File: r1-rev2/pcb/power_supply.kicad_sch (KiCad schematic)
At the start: 28 parts, among them J5 GT-BTP30003-xxxA-16A, Q3 AO3401A, U4 LM66100DCK, U5 TPS62A01DRLR, U6 TPS62A01DRLR, U7 AP2125K-3.0, U8 AP2125K-3.0, U9 TP4057

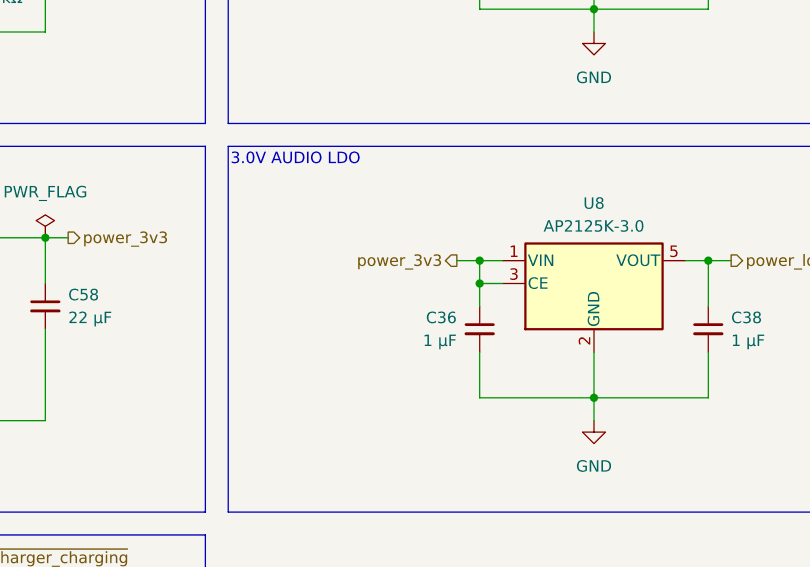
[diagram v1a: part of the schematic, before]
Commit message: R1-Rev2: use LDO enable pin to control codec AVDD supply
Now that the codec has a dedicated power supply for AVDD,
the LDO's enable pin can be used for power sequencing.
This eliminates a resistor and PMOS.
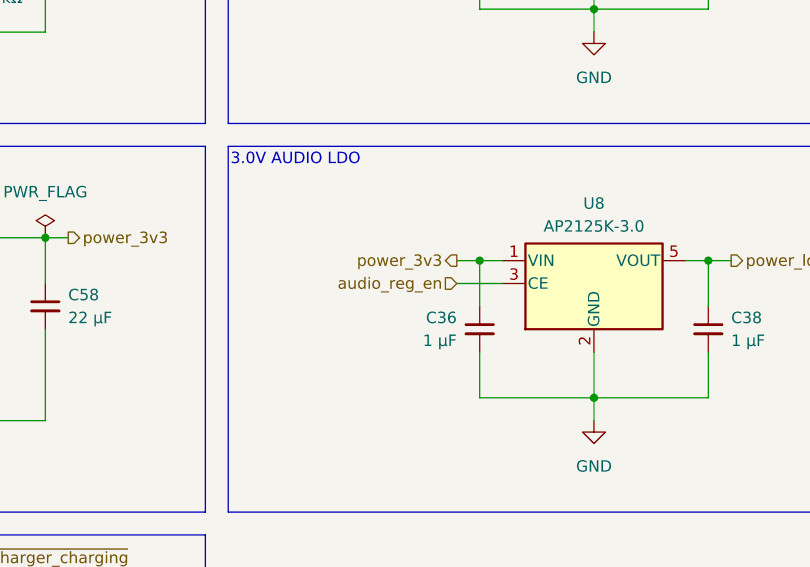
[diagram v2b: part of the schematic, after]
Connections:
- net power_3v3: no longer U8.3 (CE)
- new net audio_reg_en: U8.3 (CE)
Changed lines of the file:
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@@
-	)
-	(junction
-		(at 213.36 91.44)
-		(diameter 0)
-		(color 0 0 0 0)
 	)
 	(junction
@@
 	(wire
 		(pts
-			(xy 213.36 88.9) (xy 213.36 91.44)
+			(xy 213.36 88.9) (xy 213.36 93.98)
 		)
 		(stroke
@@
 	(wire
 		(pts
+			(xy 210.82 91.44) (xy 215.9 91.44)
+		)
+		(stroke
+			(width 0)
+			(type default)
+		)
+	)
+	(wire
+		(pts
 			(xy 121.92 106.68) (xy 132.08 106.68)
 		)
@@
 	(wire
 		(pts
-			(xy 213.36 91.44) (xy 215.9 91.44)
-		)
-		(stroke
-			(width 0)
-			(type default)
-		)
-	)
-	(wire
-		(pts
 			(xy 226.06 99.06) (xy 226.06 104.14)
 		)
@@
 		(pts
 			(xy 114.3 45.72) (xy 124.46 45.72)
-		)
-		(stroke
-			(width 0)
-			(type default)
-		)
-	)
-	(wire
-		(pts
-			(xy 213.36 91.44) (xy 213.36 93.98)
 		)
 		(stroke
@@
 		)
 	)
+	(hierarchical_label "audio_reg_en"
+		(shape input)
+		(at 210.82 91.44 180)
+		(effects
+			(font
+				(size 1.27 1.27)
+			)
+			(justify right)
+		)
+	)

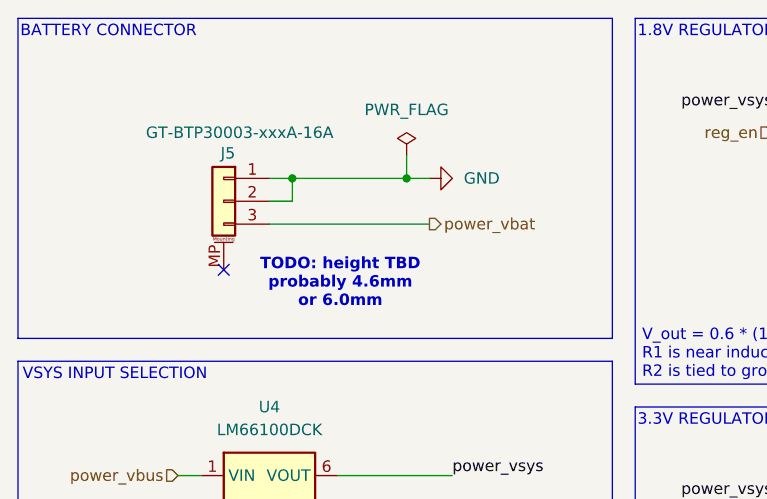
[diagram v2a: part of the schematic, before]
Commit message: R1-Rev2: add optional connection point for a wired battery
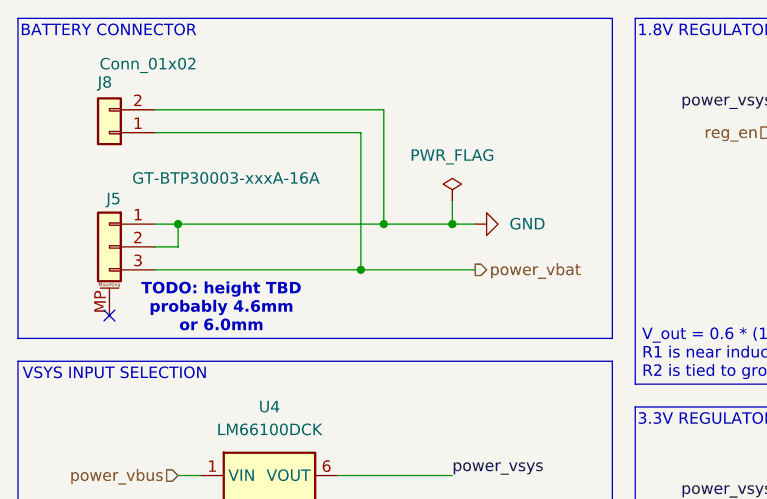
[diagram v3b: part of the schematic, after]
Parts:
- added J8: Conn_01x02, Connector_PinHeader_2.54mm:PinHeader_1x02_P2.54mm_Vertical, symbol Connector_Generic:Conn_01x02
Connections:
- net GND: now also J8.2 (Pin_2)
- net power_vbat: now also J8.1 (Pin_1)
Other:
- moved on the sheet: J5
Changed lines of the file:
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@@
 	(text "TODO: height TBD\nprobably 4.6mm\nor 6.0mm"
 		(exclude_from_sim no)
-		(at 66.294 62.484 0)
+		(at 53.086 65.278 0)
 		(effects
 			(font
@@
 	)
 	(junction
+		(at 68.58 60.96)
+		(diameter 0)
+		(color 0 0 0 0)
+	)
+	(junction
 		(at 149.86 86.36)
 		(diameter 0)
@@
 	)
 	(junction
+		(at 71.12 55.88)
+		(diameter 0)
+		(color 0 0 0 0)
+	)
+	(junction
 		(at 165.1 134.62)
 		(diameter 0)
@@
 	)
 	(junction
-		(at 73.66 50.8)
-		(diameter 0)
-		(color 0 0 0 0)
-	)
-	(junction
 		(at 149.86 106.68)
 		(diameter 0)
@@
 	)
 	(junction
-		(at 60.96 50.8)
+		(at 48.26 55.88)
 		(diameter 0)
 		(color 0 0 0 0)
@@
 	)
 	(junction
+		(at 78.74 55.88)
+		(diameter 0)
+		(color 0 0 0 0)
+	)
+	(junction
 		(at 213.36 45.72)
 		(diameter 0)
@@
 	)
 	(no_connect
-		(at 53.34 60.96)
+		(at 40.64 66.04)
 	)
 	(wire
@@
 	(wire
 		(pts
-			(xy 73.66 48.26) (xy 73.66 50.8)
-		)
-		(stroke
-			(width 0)
-			(type default)
-		)
-	)
-	(wire
-		(pts
 			(xy 132.08 106.68) (xy 132.08 109.22)
 		)
@@
 	(wire
 		(pts
+			(xy 45.72 43.18) (xy 71.12 43.18)
+		)
+		(stroke
+			(width 0)
+			(type default)
+		)
+	)
+	(wire
+		(pts
 			(xy 238.76 45.72) (xy 241.3 45.72)
 		)
@@
 	(wire
 		(pts
+			(xy 45.72 45.72) (xy 68.58 45.72)
+		)
+		(stroke
+			(width 0)
+			(type default)
+		)
+	)
+	(wire
+		(pts
 			(xy 210.82 88.9) (xy 213.36 88.9)
 		)
@@
 	(wire
 		(pts
-			(xy 58.42 55.88) (xy 76.2 55.88)
+			(xy 45.72 60.96) (xy 68.58 60.96)
 		)
 		(stroke
@@
 	(wire
 		(pts
+			(xy 78.74 55.88) (xy 78.74 53.34)
+		)
+		(stroke
+			(width 0)
+			(type default)
+		)
+	)
+	(wire
+		(pts
 			(xy 127 149.86) (xy 139.7 149.86)
 		)
@@
 	(wire
 		(pts
+			(xy 78.74 55.88) (xy 81.28 55.88)
+		)
+		(stroke
+			(width 0)
+			(type default)
+		)
+	)
+	(wire
+		(pts
 			(xy 144.78 96.52) (xy 149.86 96.52)
 		)
@@
 	(wire
 		(pts
-			(xy 58.42 53.34) (xy 60.96 53.34)
+			(xy 45.72 58.42) (xy 48.26 58.42)
 		)
 		(stroke
@@
 	(wire
 		(pts
-			(xy 60.96 50.8) (xy 73.66 50.8)
+			(xy 48.26 55.88) (xy 71.12 55.88)
 		)
 		(stroke
@@
 	(wire
 		(pts
-			(xy 73.66 50.8) (xy 76.2 50.8)
+			(xy 152.4 53.34) (xy 152.4 55.88)
 		)
 		(stroke
@@
 	(wire
 		(pts
-			(xy 152.4 53.34) (xy 152.4 55.88)
+			(xy 165.1 106.68) (xy 149.86 106.68)
 		)
 		(stroke
@@
 	(wire
 		(pts
-			(xy 165.1 106.68) (xy 149.86 106.68)
+			(xy 114.3 43.18) (xy 121.92 43.18)
 		)
 		(stroke
@@
 	(wire
 		(pts
-			(xy 114.3 43.18) (xy 121.92 43.18)
+			(xy 149.86 93.98) (xy 149.86 96.52)
 		)
 		(stroke
@@
 	(wire
 		(pts
-			(xy 149.86 93.98) (xy 149.86 96.52)
+			(xy 68.58 45.72) (xy 68.58 60.96)
 		)
 		(stroke
@@
 	(wire
 		(pts
-			(xy 58.42 50.8) (xy 60.96 50.8)
+			(xy 45.72 55.88) (xy 48.26 55.88)
 		)
 		(stroke
@@
 	(wire
 		(pts
+			(xy 71.12 55.88) (xy 78.74 55.88)
+		)
+		(stroke
+			(width 0)
+			(type default)
+		)
+	)
+	(wire
+		(pts
 			(xy 165.1 91.44) (xy 165.1 86.36)
 		)
@@
 	(wire
 		(pts
-			(xy 60.96 50.8) (xy 60.96 53.34)
+			(xy 48.26 55.88) (xy 48.26 58.42)
 		)
 		(stroke
@@
 	(wire
 		(pts
+			(xy 68.58 60.96) (xy 81.28 60.96)
+		)
+		(stroke
+			(width 0)
+			(type default)
+		)
+	)
+	(wire
+		(pts
+			(xy 71.12 43.18) (xy 71.12 55.88)
+		)
+		(stroke
+			(width 0)
+			(type default)
+		)
+	)
+	(wire
+		(pts
 			(xy 66.04 83.82) (xy 78.74 83.82)
 		)
@@
 	(hierarchical_label "power_vbat"
 		(shape output)
-		(at 76.2 55.88 0)
+		(at 81.28 60.96 0)
 		(effects
 			(font
@@
 	(symbol
 		(lib_id "echoplayer:GT-BTP30003")
-		(at 53.34 53.34 0)
+		(at 40.64 58.42 0)
 		(mirror y)
 		(unit 1)
@@
 		(dnp no)
 		(property "Reference" "J5"
-			(at 54.61 48.006 0)
+			(at 41.91 53.086 0)
 			(effects
 				(font
@@
 		)
 		(property "Value" "GT-BTP30003-xxxA-16A"
-			(at 65.532 45.72 0)
+			(at 64.008 50.8 0)
 			(effects
 				(font
@@
 		)
 		(property "Footprint" "echoplayer:Conn_GT-BTP30003-xxxxA-016A"
-			(at 53.34 53.34 0)
+			(at 40.64 58.42 0)
 			(effects
 				(font
@@
 		)
 		(property "Datasheet" "https://www.lcsc.com/datasheet/lcsc_datasheet_2409091552_G-Switch-GT-BTP30003-0460A-016A_C41378737.pdf"
-			(at 53.34 53.34 0)
+			(at 40.64 58.42 0)
 			(effects
 				(font
@@
 		)
 		(property "Description" "3-pin blade/shrapnel battery connector, SMD, vertical mount with mounting pin"
-			(at 53.34 53.34 0)
+			(at 40.64 58.42 0)
 			(effects
 				(font
@@
 	)
 	(symbol
+		(lib_id "Connector_Generic:Conn_01x02")
+		(at 40.64 45.72 180)
+		(unit 1)
+		(exclude_from_sim no)
+		(in_bom yes)
+		(on_board yes)
+		(dnp no)
+		(property "Reference" "J8"
+			(at 40.132 40.132 0)
+			(effects
+				(font
+					(size 1.27 1.27)
+				)
+			)
+		)
+		(property "Value" "Conn_01x02"
+			(at 44.958 38.1 0)
+			(effects
+				(font
+					(size 1.27 1.27)
+				)
+			)
+		)
+		(property "Footprint" "Connector_PinHeader_2.54mm:PinHeader_1x02_P2.54mm_Vertical"
+			(at 40.64 45.72 0)
+			(effects
+				(font
+					(size 1.27 1.27)
+				)
+				(hide yes)
+			)
+		)
+		(property "Datasheet" "~"
+			(at 40.64 45.72 0)
+			(effects
+				(font
+					(size 1.27 1.27)
+				)
+				(hide yes)
+			)
+		)
+		(property "Description" "Generic connector, single row, 01x02, script generated (kicad-library-utils/schlib/autogen/connector/)"
+			(at 40.64 45.72 0)
+			(effects
+				(font
+					(size 1.27 1.27)
+				)
+				(hide yes)
+			)
+		)
+		(pin "2"
+		)
+		(pin "1"
+		)
+		(instances
+			(project ""
+				(path "/aa241847-30f4-429d-a148-6a6e39ba98e0/48d39f5c-11a4-46cd-927a-56a9c6ae42fa"
+					(reference "J8")
+					(unit 1)
+				)
+			)
+		)
+	)
+	(symbol
 		(lib_id "echoplayer:AP2125K-3.0")
 		(at 226.06 91.44 0)
@@
 	(symbol
 		(lib_id "power:GND")
-		(at 76.2 50.8 90)
+		(at 81.28 55.88 90)
 		(unit 1)
 		(exclude_from_sim no)
@@
 		(fields_autoplaced yes)
 		(property "Reference" "#PWR0171"
-			(at 82.55 50.8 0)
+			(at 87.63 55.88 0)
 			(effects
 				(font
@@
 		)
 		(property "Value" "GND"
-			(at 80.01 50.7999 90)
+			(at 85.09 55.8799 90)
 			(effects
 				(font
@@
 		)
 		(property "Footprint" ""
-			(at 76.2 50.8 0)
+			(at 81.28 55.88 0)
 			(effects
 				(font
@@
 		)
 		(property "Datasheet" ""
-			(at 76.2 50.8 0)
+			(at 81.28 55.88 0)
 			(effects
 				(font
@@
 		)
 		(property "Description" "Power symbol creates a global label with name \"GND\" , ground"
-			(at 76.2 50.8 0)
+			(at 81.28 55.88 0)
 			(effects
 				(font
@@
 	(symbol
 		(lib_id "power:PWR_FLAG")
-		(at 73.66 48.26 0)
+		(at 78.74 53.34 0)
 		(unit 1)
 		(exclude_from_sim no)
@@
 		(fields_autoplaced yes)
 		(property "Reference" "#FLG0108"
-			(at 73.66 46.355 0)
+			(at 78.74 51.435 0)
 			(effects
 				(font
@@
 		)
 		(property "Value" "PWR_FLAG"
-			(at 73.66 43.18 0)
+			(at 78.74 48.26 0)
 			(effects
 				(font
@@
 		)
 		(property "Footprint" ""
-			(at 73.66 48.26 0)
+			(at 78.74 53.34 0)
 			(effects
 				(font
@@
 		)
 		(property "Datasheet" "~"
-			(at 73.66 48.26 0)
+			(at 78.74 53.34 0)
 			(effects
 				(font
@@
 		)
 		(property "Description" "Special symbol for telling ERC where power comes from"
-			(at 73.66 48.26 0)
+			(at 78.74 53.34 0)
 			(effects
 				(font

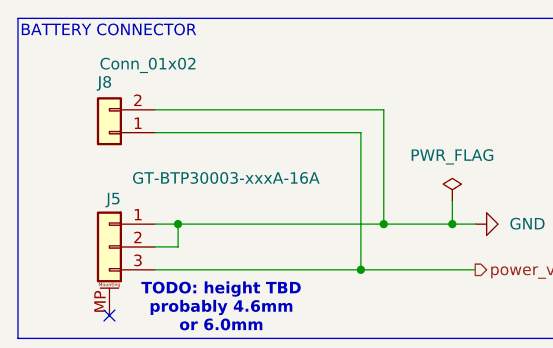
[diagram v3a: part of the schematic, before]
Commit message: R1-Rev2: fix/improve fab layer text on a few footprints
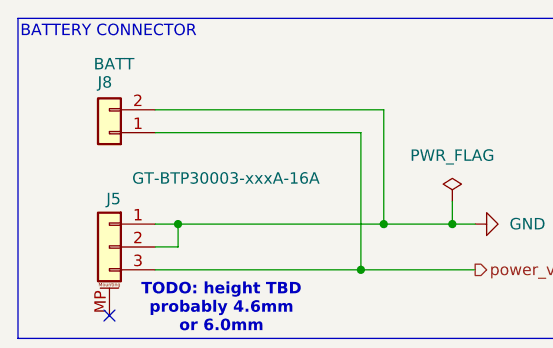
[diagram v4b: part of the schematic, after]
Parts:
- J8: value Conn_01x02 -> BATT
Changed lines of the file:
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@@
 			)
 		)
-		(property "Value" "Conn_01x02"
-			(at 44.958 38.1 0)
+		(property "Value" "BATT"
+			(at 41.148 38.1 0)
 			(effects
 				(font
